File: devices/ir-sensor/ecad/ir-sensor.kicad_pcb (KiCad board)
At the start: 2 copper layers, 25 x 8 mm, 6 parts, among them J1 SM03B-SRSS-TB, U1 EE-SY1201

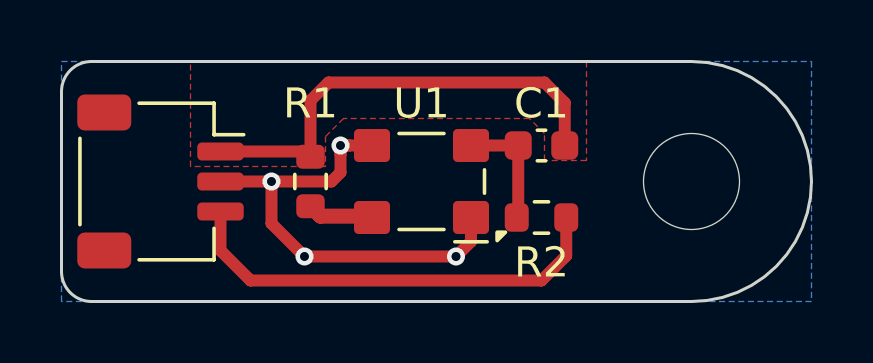
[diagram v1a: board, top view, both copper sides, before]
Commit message: [IR Sensor] Updates to Allow Mixed Purpose.
* Indicate that only part could be populated to have:
  * An IR emitter
  * An IR Phototransistor
  * Both (reflective mode)
* Turn the IR Module so if flipped vertically barrier and IR are aligned.
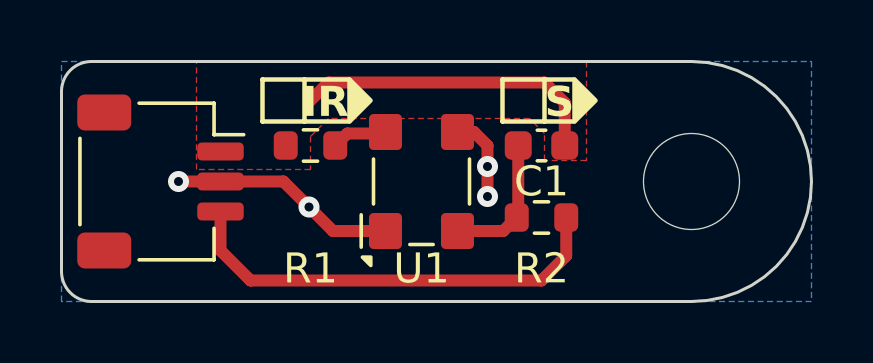
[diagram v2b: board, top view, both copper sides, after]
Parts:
- moved R1 1.20 mm to (87.3, 58.8), turned to 0 degrees
- turned U1 to 90 degrees
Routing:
- net GND: track 15.6 -> 10.5 mm
- net +3V3: track 15.4 -> 10.4 mm
- net /OUT_H: track 4.00 -> 4.58 mm
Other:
- board text added: "IR"
- board text added: "S"

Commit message: Adds license and output for IR Sensor
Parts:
- added REF**: OSHW-Logo_5.7x6mm_SilkScreen, Symbol:OSHW-Logo_5.7x6mm_SilkScreen, B.Cu at (83.0, 60.2)
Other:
- board text added: "IR Sensor Rev A"
